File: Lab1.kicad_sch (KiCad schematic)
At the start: 14 parts, among them J1 Conn_02x05_Counter_Clockwise, SW1 SW_Nidec_CAS-120A1, SW2 CK_KMS2xxG, SW3 CK_KMS2xxG, U1 STM32F407VGTx, Y1 Crystal

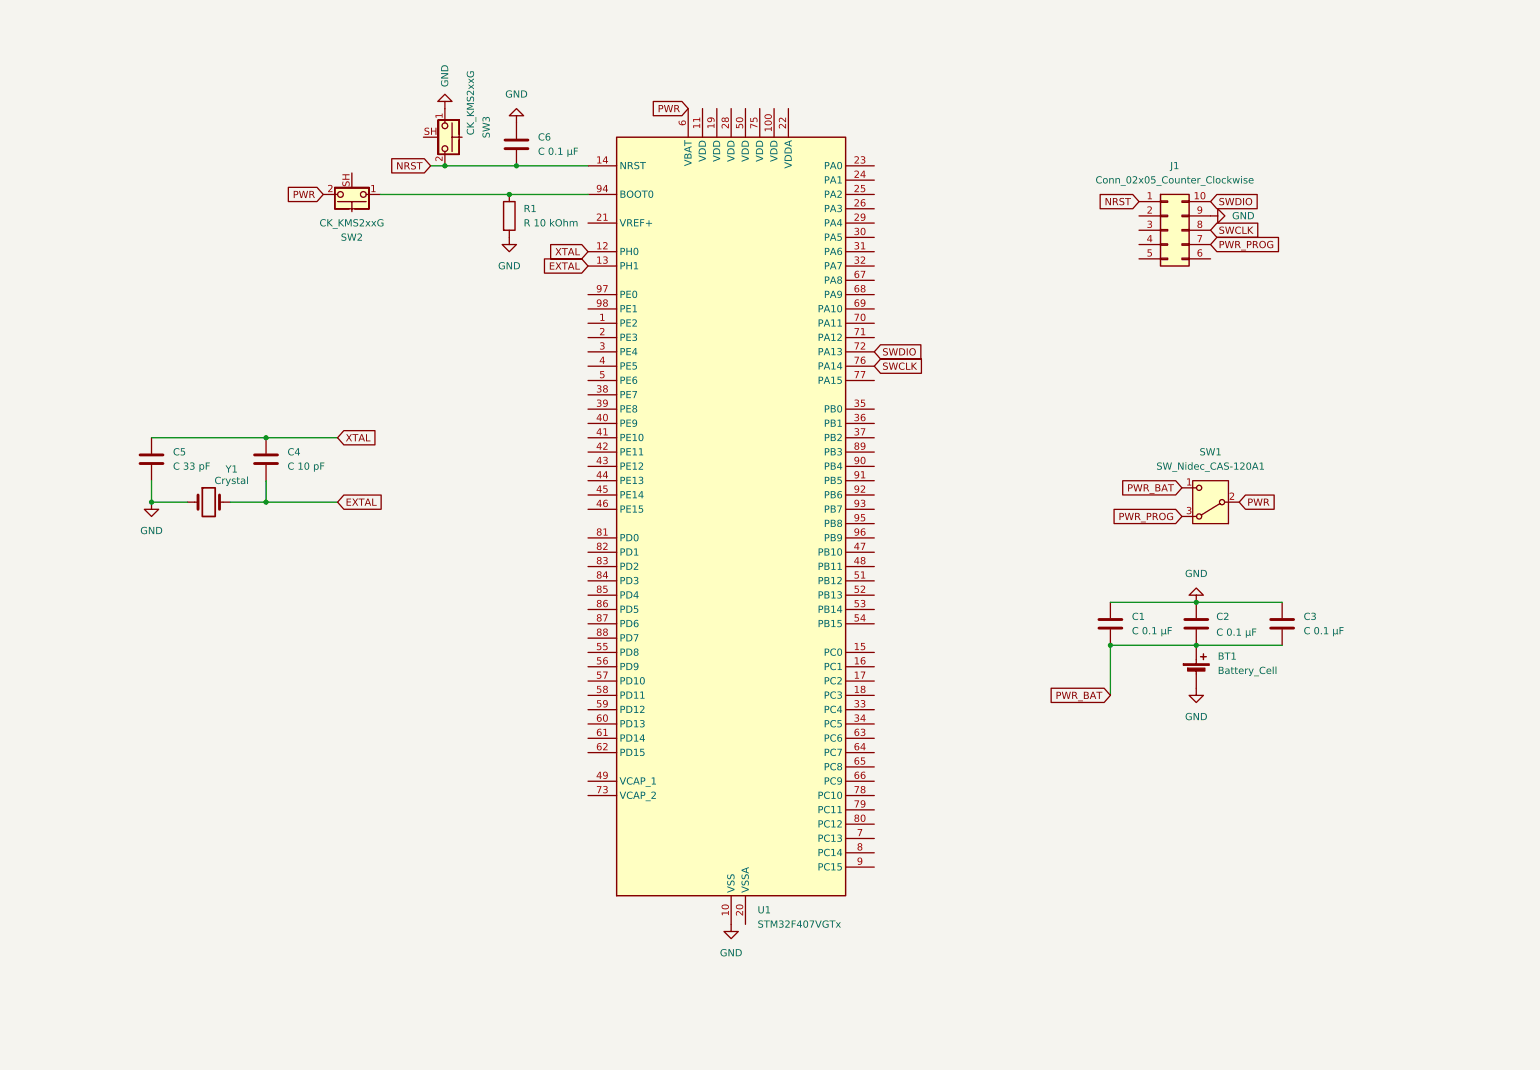
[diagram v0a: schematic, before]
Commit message: feat: Update footprints for buttons and add Libs
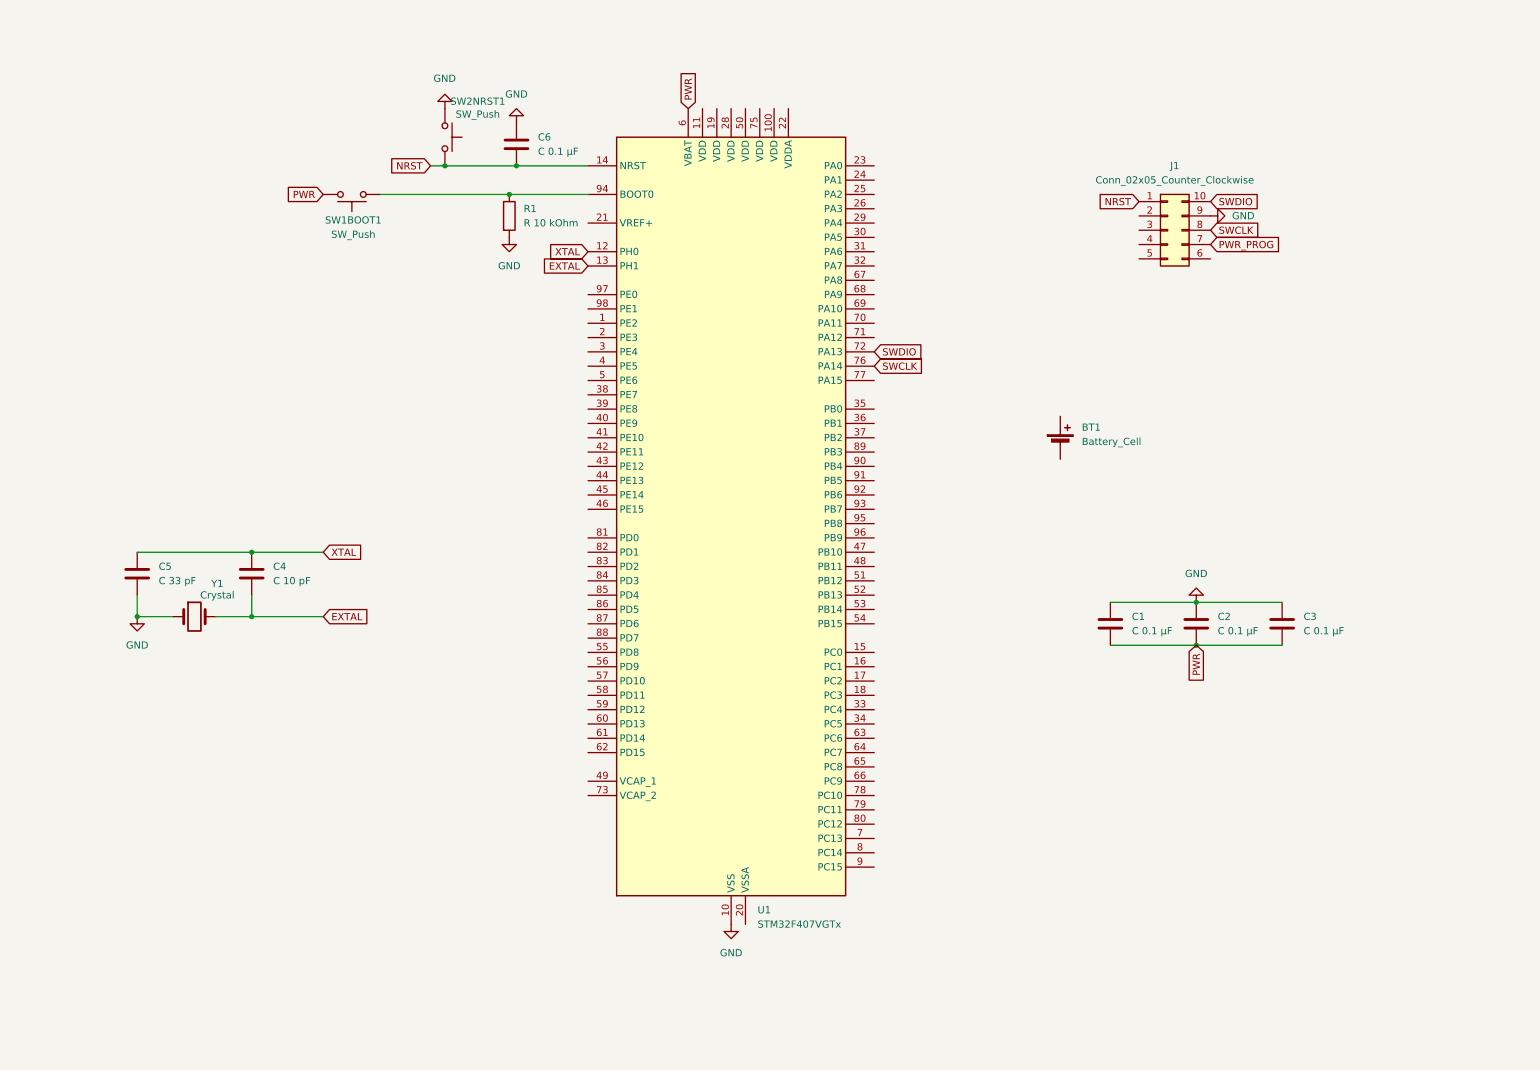
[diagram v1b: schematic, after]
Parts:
- removed SW1: SW_Nidec_CAS-120A1, Button_Switch_SMD:Nidec_Copal_CAS-120A, symbol Switch:SW_Nidec_CAS-120A1
- removed SW2, SW3: CK_KMS2xxG, Button_Switch_SMD:SW_SPST_CK_KMS2xxGP, symbol Switch:CK_KMS2xxG
- added SW1BOOT1, SW2NRST1: SW_Push, Button_Switch_THT:SW_PUSH_6mm, symbol Switch:SW_Push
- C2, C3: footprint (none) -> Capacitor_SMD:C_0805_2012Metric_Pad1.18x1.45mm_HandSolder
- J1: footprint Connector_PinHeader_1.00mm:PinHeader_2x05_P1.00mm_Vertical -> Connector_PinHeader_2.54mm:PinHeader_2x05_P2.54mm_Vertical
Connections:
- net GND: now also SW2NRST1.1; no longer BT1.2 (-)
- net NRST: now also SW2NRST1.2
- net PWR: now also C1.2, C2.2, C3.2, SW1BOOT1.2
- net at R1.1, U1.94 (BOOT0): now also SW1BOOT1.1
- removed net PWR_BAT: BT1.1 (+), C1.2, C2.2, C3.2
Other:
- moved on the sheet: C4, C5, Y1

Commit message: fix: add ERC power input
feat: structure the diagram into modules

refactor: change global labels to local

feat: add PCB board

feat: make ERC adnd DRC check
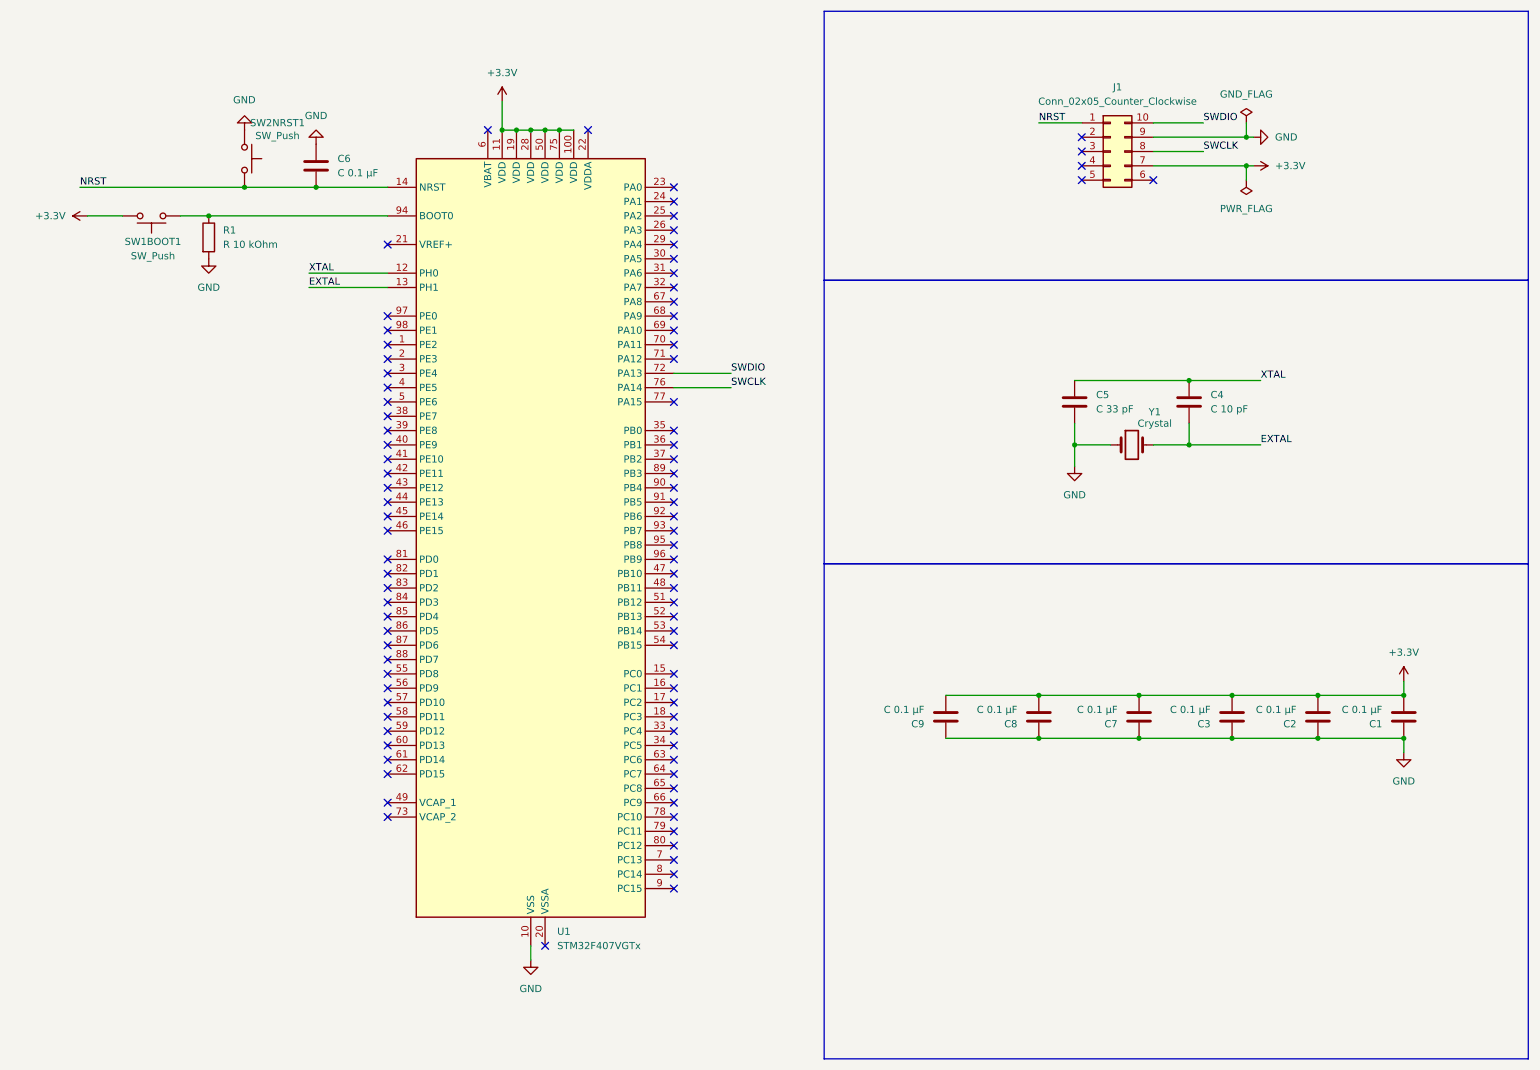
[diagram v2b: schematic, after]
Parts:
- removed BT1: Battery_Cell, symbol Device:Battery_Cell
- added C7, C8, C9: C 0.1 μF, Capacitor_SMD:C_0805_2012Metric_Pad1.18x1.45mm_HandSolder, symbol Device:C
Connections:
- net PWR_PROG is gone; now on net +3.3V: J1.7 (Pin_7)
- net GND: now also C7.1, C8.1, C9.1
- net +3.3V: now reaches U1.100 (VDD)
- net +3.3V: now also C1.2, C2.2, C3.2, SW1BOOT1.2, U1.11 (VDD), U1.19 (VDD), U1.28 (VDD), U1.50 (VDD), U1.75 (VDD), C7.2, C8.2, C9.2
- removed net PWR: C1.2, C2.2, C3.2, SW1BOOT1.2, U1.6 (VBAT)
- no-connect marks 0 -> 89
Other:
- moved on the sheet: C1, C2, C3, C4, C5, C6, J1, R1, SW1BOOT1, SW2NRST1, U1, Y1

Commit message: chore: add stamp
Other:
- company: (none) -> SQUAD4 Inc.
- title: (none) -> PCB001
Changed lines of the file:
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@@
 	(generator_version "9.0")
 	(paper "A4")
+	(title_block
+		(title "PCB001")
+		(rev "0.1")
+		(company "SQUAD4 Inc.")
+	)
 	(rectangle
 		(start 160.02 109.982)

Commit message: feat: add GPIO pins
feat: add user buttons

feat: add user LED

feat: add user potentiometer
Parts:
- added Button_1, Button_2: SW_Push, Button_Switch_THT:SW_PUSH_6mm, symbol Switch:SW_Push
- added D1: LED Blue, LED_SMD:LED_0805_2012Metric, symbol Device:LED
- added D2: LED Red, LED_SMD:LED_0805_2012Metric, symbol Device:LED
- added D3: LED Orange, LED_SMD:LED_0805_2012Metric, symbol Device:LED
- added D4: LED Green, LED_SMD:LED_0805_2012Metric, symbol Device:LED
- added R2: R 30 Ohm, Resistor_SMD:R_0805_2012Metric_Pad1.20x1.40mm_HandSolder, symbol Device:R
- added R3, R4, R5: R 100 Ohm, Resistor_SMD:R_0805_2012Metric_Pad1.20x1.40mm_HandSolder, symbol Device:R
- added R6, R7: R 10 kOhm, Resistor_SMD:R_0805_2012Metric_Pad1.20x1.40mm_HandSolder, symbol Device:R
- added RV1, RV2: 10 kOhm, Potentiometer_THT:Potentiometer_ACP_CA9-V10_Vertical, symbol Device:R_Potentiometer_Small
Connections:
- net +3.3V: now also Button_1.1, R7.2, RV1.1, RV2.1
- net GND: now also Button_2.1, D1.2 (A), D2.2 (A), D3.2 (A), D4.2 (A), R6.2, RV1.3, RV2.3
- net ADC_1: now reaches U1.15 (PC0)
- net ADC_1: now also RV1.2
- net ADC_2: now reaches U1.16 (PC1)
- net ADC_2: now also RV2.2
- net UButton_1: now reaches U1.57 (PD10)
- net UButton_1: now also Button_1.2, R6.1
- net UButton_2: now reaches U1.58 (PD11)
- net UButton_2: now also Button_2.2, R7.1
- net LED_Green: now reaches U1.59 (PD12)
- net LED_Green: now also R3.1
- net LED_Orange: now reaches U1.60 (PD13)
- net LED_Orange: now also R4.1
- net LED_Red: now reaches U1.61 (PD14)
- net LED_Red: now also R5.1
- net LED_Blue: now reaches U1.62 (PD15)
- net LED_Blue: now also R2.1
- new net: D2.1 (K), R5.2
- new net: D4.1 (K), R3.2
- new net: D1.1 (K), R2.2
- new net: D3.1 (K), R4.2
- no-connect marks 89 -> 81
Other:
- moved on the sheet: C1, C2, C3, C4, C5, C6, C7, C8, C9, J1, R1, SW1BOOT1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
